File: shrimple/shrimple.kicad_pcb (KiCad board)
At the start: 2 copper layers, 105 parts, among them U3 Sparkfun_Pro_Micro

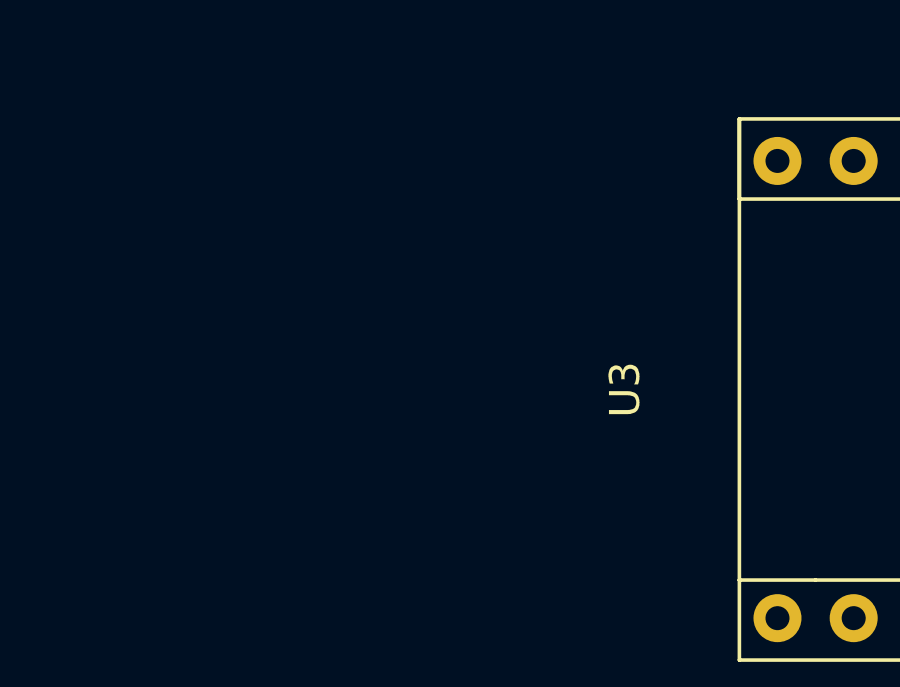
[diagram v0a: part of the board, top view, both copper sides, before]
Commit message: added LED circuit
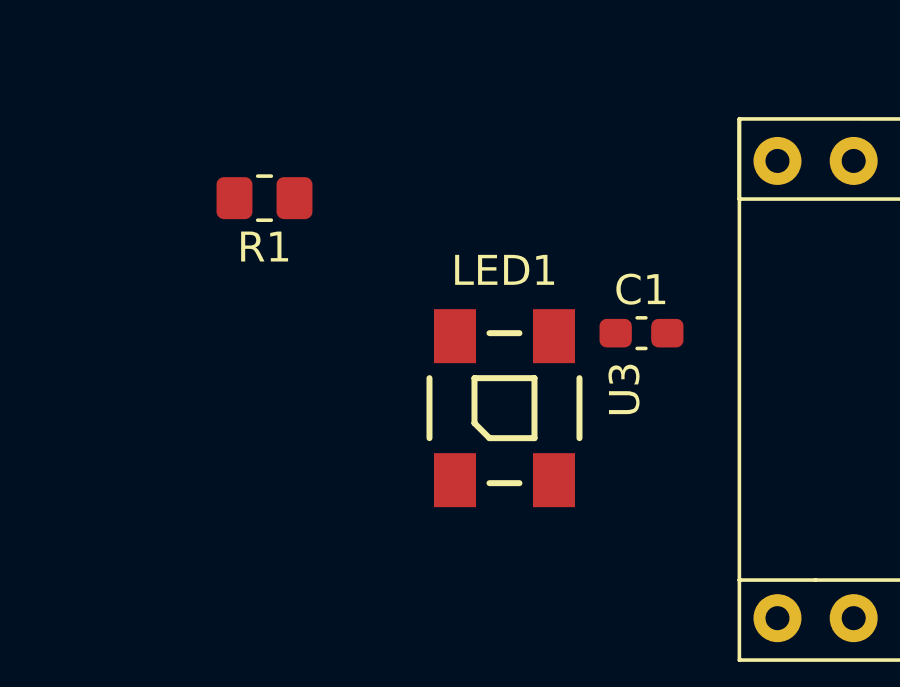
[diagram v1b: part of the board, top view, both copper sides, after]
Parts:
- added C1: C_Small, Capacitor_SMD:C_0603_1608Metric_Pad1.08x0.95mm_HandSolder, F.Cu at (241.6, 41.0)
- added LED1: WS2812B, ws2812:WS2812B, F.Cu at (237.0, 43.5)
- added R1: R_Small, Resistor_SMD:R_0805_2012Metric_Pad1.20x1.40mm_HandSolder, F.Cu at (229.0, 36.5)
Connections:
- U3 pad 15: unconnected-(U3-D14-Pad15) -> ROW0
- U3 pad 16: ROW0 -> ROW1
- U3 pad 17: ROW1 -> ROW2
- U3 pad 18: ROW2 -> ROW3
- U3 pad 19: ROW3 -> ROW4
- U3 pad 20: ROW4 -> RGBDATA
- U3 pad 23: unconnected-(U3-GND-Pad23) -> GND
- U3 pad 24: unconnected-(U3-RAW-Pad24) -> +5V
- U3 pad 3: unconnected-(U3-GND-Pad3) -> GND
- U3 pad 4: unconnected-(U3-GND-Pad4) -> GND

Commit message: added LED, routing attempt the first
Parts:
- R1: moved to B.Cu
- moved LED1 67.2 mm to (170.0, 38.5)
- moved C1 66.7 mm to (175.0, 37.0), turned to -90 degrees
- moved R1 65.0 mm to (164.0, 37.0), turned to -90 degrees
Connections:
- U3 pad 10: COL4 -> COL3
- U3 pad 11: COL3 -> COL4
- U3 pad 12: COL2 -> COL5
- U3 pad 13: COL0 -> COL10
- U3 pad 14: COL1 -> COL9
- U3 pad 15: ROW0 -> COL8
- U3 pad 16: ROW1 -> COL7
- U3 pad 17: ROW2 -> COL6
- U3 pad 18: ROW3 -> ROW1
- U3 pad 19: ROW4 -> ROW2
- U3 pad 2: COL10 -> ROW3
- U3 pad 5: COL9 -> ROW4
- U3 pad 6: COL8 -> ROW0
- U3 pad 7: COL7 -> COL0
- U3 pad 8: COL6 -> COL1
- U3 pad 9: COL5 -> COL2
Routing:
- net ROW0: track 0.00 -> 372.6 mm, vias 0 -> 2
- net ROW4: track 0.00 -> 330.9 mm
- net COL0: track 0.00 -> 310.0 mm
- net ROW3: track 0.00 -> 296.1 mm
- net COL1: track 0.00 -> 290.0 mm
- net COL2: track 0.00 -> 266.1 mm
- net ROW2: track 0.00 -> 263.4 mm
- net COL4: track 0.00 -> 225.7 mm
- net ROW1: track 0.00 -> 225.0 mm
- net COL3: track 0.00 -> 224.2 mm
- net COL5: track 0.00 -> 179.3 mm
- net COL6: track 0.00 -> 176.5 mm
- net GND: track 0.00 -> 138.7 mm, vias 0 -> 2
- net COL7: track 0.00 -> 131.8 mm
- net COL8: track 0.00 -> 130.0 mm
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
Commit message: added ground fills and vias
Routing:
- net GND: track 138.7 -> 0.00 mm, vias 2 -> 45
- added copper zone on B.Cu, net GND
- added copper zone on F.Cu, net GND
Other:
- board outline added: 249.2 x 103.4 mm

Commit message: added art
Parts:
- added G***: LOGO, LOGO, F.Cu at (199.2, 40.4)
- added G***: LOGO, LOGO, B.Cu at (211.0, 44.6)
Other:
- board text added: "design by anchovie https://anchovie.art"
- board text added: "keeb it shrimple!"

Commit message: fixed art and weird row trace
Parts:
- added H1: MountingHole, MountingHole:MountingHole_2.2mm_M2_Pad_TopOnly, F.Cu at (46.2, 49.0)
- added H2: MountingHole, MountingHole:MountingHole_2.2mm_M2_Pad_TopOnly, F.Cu at (51.6, 110.2)
- added H3: MountingHole, MountingHole:MountingHole_2.2mm_M2_Pad_TopOnly, F.Cu at (145.8, 112.2)
- added H4: MountingHole, MountingHole:MountingHole_2.2mm_M2_Pad_TopOnly, F.Cu at (238.6, 55.8)
- added H5: MountingHole, MountingHole:MountingHole_2.2mm_M2_Pad_TopOnly, F.Cu at (255.8, 109.4)
- added H6: MountingHole, MountingHole:MountingHole_2.2mm_M2_Pad_TopOnly, F.Cu at (154.6, 42.6)
- moved G*** 3.72 mm to (208.0, 42.4)
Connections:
- U3 pad 10: COL3 -> COL4
- U3 pad 11: COL4 -> COL5
- U3 pad 12: COL5 -> ROW0
- U3 pad 6: ROW0 -> COL0
- U3 pad 7: COL0 -> COL1
- U3 pad 8: COL1 -> COL2
- U3 pad 9: COL2 -> COL3
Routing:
- net ROW0: track 372.6 -> 356.8 mm, vias 2 -> 3
- net COL4: track 225.7 -> 228.3 mm
- net COL2: track 266.1 -> 268.6 mm
- net COL0: track 310.0 -> 312.5 mm
- net COL5: track 179.3 -> 181.8 mm
- net COL1: track 290.0 -> 292.5 mm
- net COL3: track 224.2 -> 226.7 mm
- net GND: vias 45 -> 43
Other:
- board size 249.2 x 103.4 mm -> 249.2 x 106.2 mm

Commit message: fixed spacebar placement fuck my stupid baka life
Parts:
- LED1: value WS2812B -> VAL**
- moved D47 3.42 mm to (129.5, 125.0)
- moved MX47 3.26 mm to (121.5, 123.8)
- moved MX48 3.25 mm to (169.1, 123.8)
- moved D48 3.25 mm to (177.2, 125.0)
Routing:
- net ROW4: track 330.9 -> 332.9 mm
- net COL6: track 176.5 -> 177.7 mm
- net COL4: track 228.3 -> 229.5 mm
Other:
- board size 249.2 x 106.2 mm -> 249.2 x 105.6 mm

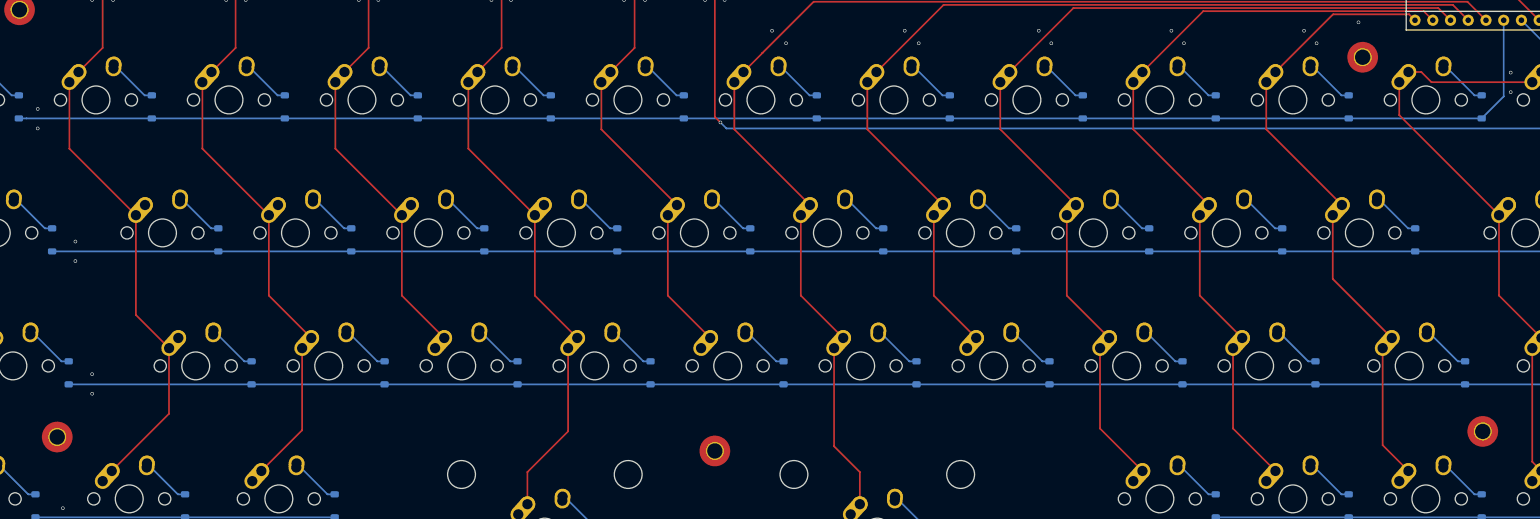
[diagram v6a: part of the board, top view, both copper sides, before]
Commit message: moved mounting holes
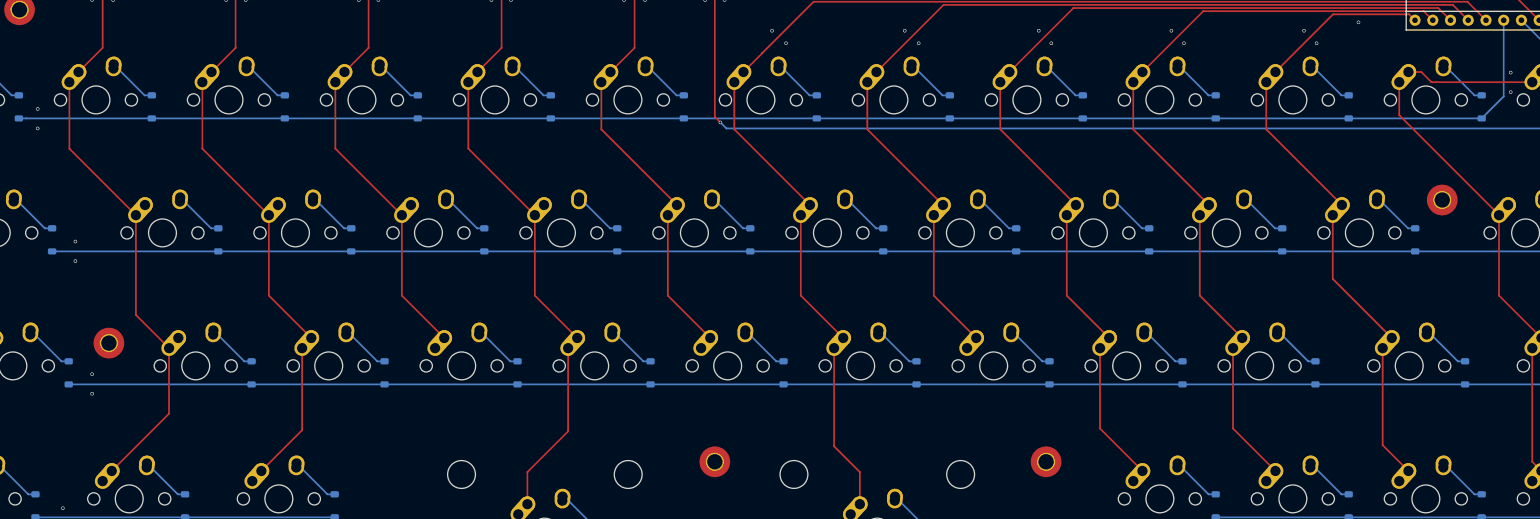
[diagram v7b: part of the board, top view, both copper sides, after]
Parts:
- moved H4 73.6 mm to (193.2, 113.8)
- moved H5 33.7 mm to (250.0, 76.2)
- moved H2 15.4 mm to (59.0, 96.8)
- moved H3 1.55 mm to (145.8, 113.8)
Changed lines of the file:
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@@
 	(footprint "MountingHole:MountingHole_2.2mm_M2_Pad_TopOnly"
 		(layer "F.Cu")
-		(at 145.8 112.2)
+		(at 145.8 113.75)
 		(descr "Mounting Hole 2.2mm, M2")
 		(tags "mounting hole 2.2mm m2")
@@
 	(footprint "MountingHole:MountingHole_2.2mm_M2_Pad_TopOnly"
 		(layer "F.Cu")
-		(at 255.8 109.4)
+		(at 250 76.25)
 		(descr "Mounting Hole 2.2mm, M2")
 		(tags "mounting hole 2.2mm m2")
@@
 	(footprint "MountingHole:MountingHole_2.2mm_M2_Pad_TopOnly"
 		(layer "F.Cu")
-		(at 238.6 55.8)
+		(at 193.25 113.75)
 		(descr "Mounting Hole 2.2mm, M2")
 		(tags "mounting hole 2.2mm m2")
@@
 	(footprint "MountingHole:MountingHole_2.2mm_M2_Pad_TopOnly"
 		(layer "F.Cu")
-		(at 51.6 110.2)
+		(at 59 96.75)
 		(descr "Mounting Hole 2.2mm, M2")
 		(tags "mounting hole 2.2mm m2")
